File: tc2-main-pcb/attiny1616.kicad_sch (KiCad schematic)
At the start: 20 parts, among them J104 Conn_02x03_Odd_Even, U117 ATtiny1616-M

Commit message: Updated to use field LCSC Part instead of LCSC for the JLCPCB part number
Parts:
- C146, C166: LCSC C16772 -> (none); LCSC Part (none) -> C16772
- C165, C167: LCSC C1555 -> (none); LCSC Part (none) -> C1555
- J104: LCSC C3975129 -> (none); LCSC Part (none) -> C3975129
- R146, R150: LCSC C326730 -> (none); LCSC Part (none) -> C326730
- R147, R151: LCSC C25744 -> (none); LCSC Part (none) -> C25744
- R149: LCSC C25741 -> (none); LCSC Part (none) -> C25741
- R152: LCSC C445619 -> (none); LCSC Part (none) -> C445619
- R153: LCSC C445618 -> (none); LCSC Part (none) -> C445618
- R154, R155, R156: LCSC C11702 -> (none); LCSC Part (none) -> C11702
- R160: LCSC C319591 -> (none); LCSC Part (none) -> C319591
- U117: LCSC C507118 -> (none); LCSC Part (none) -> C507118
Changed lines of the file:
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@@
 			)
 		)
-		(property "LCSC" "C326730"
+		(property "LCSC Part" "C326730"
 			(at 270.51 99.06 0)
 			(effects
@@
 			)
 		)
-		(property "LCSC" "C445618"
+		(property "LCSC Part" "C445618"
 			(at 270.51 118.11 0)
 			(effects
@@
 			)
 		)
-		(property "LCSC" "C11702"
+		(property "LCSC Part" "C11702"
 			(at 62.23 129.54 0)
 			(effects
@@
 			)
 		)
-		(property "LCSC" "C326730"
+		(property "LCSC Part" "C326730"
 			(at 270.51 68.58 0)
 			(effects
@@
 			)
 		)
-		(property "LCSC" "C11702"
+		(property "LCSC Part" "C11702"
 			(at 62.23 124.46 0)
 			(effects
@@
 			)
 		)
-		(property "LCSC" "C445619"
+		(property "LCSC Part" "C445619"
 			(at 270.51 109.22 0)
 			(effects
@@
 			)
 		)
-		(property "LCSC" "C3975129"
+		(property "LCSC Part" "C3975129"
 			(at 215.9 143.51 0)
 			(effects
@@
 			)
 		)
-		(property "LCSC" "C1555"
+		(property "LCSC Part" "C1555"
 			(at 250.19 110.49 0)
 			(effects
@@
 			)
 		)
-		(property "LCSC" "C25744"
+		(property "LCSC Part" "C25744"
 			(at 246.38 73.66 0)
 			(effects
@@
 			)
 		)
-		(property "LCSC" "C16772"
+		(property "LCSC Part" "C16772"
 			(at 224.79 149.86 0)
 			(effects
@@
 			)
 		)
-		(property "LCSC" "C25744"
+		(property "LCSC Part" "C25744"
 			(at 245.11 104.14 0)
 			(effects
@@
 			)
 		)
-		(property "LCSC" "C25741"
+		(property "LCSC Part" "C25741"
 			(at 147.32 93.98 0)
 			(effects
@@
 			)
 		)
-		(property "LCSC" "C16772"
+		(property "LCSC Part" "C16772"
 			(at 106.68 91.44 0)
 			(effects
@@
 			)
 		)
-		(property "LCSC" "C11702"
+		(property "LCSC Part" "C11702"
 			(at 62.23 132.08 0)
 			(effects
@@
 			)
 		)
-		(property "LCSC" "C1555"
+		(property "LCSC Part" "C1555"
 			(at 251.46 78.74 0)
 			(effects
@@
 			)
 		)
-		(property "LCSC" "C319591"
+		(property "LCSC Part" "C319591"
 			(at 270.51 78.74 0)
 			(effects
@@
 			)
 		)
-		(property "LCSC" "C507118"
+		(property "LCSC Part" "C507118"
 			(at 110.49 119.38 0)
 			(effects

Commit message: Tidy up
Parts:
- removed C146: 220nF, Capacitor_SMD:C_0402_1005Metric, symbol Device:C_Small
- removed H107, H108: MountingHole, cacophony-library:MountingHole_2.2mm_M2, symbol Mechanical:MountingHole
- removed J104: Conn_02x03_Odd_Even, cacophony-library:mic-pcb, symbol Connector_Generic:Conn_02x03_Odd_Even
- added LED1: NH-B1515RGBA-HF, cacophony-library:LED-ARRAY-SMD_4P-L1.6-W1.5-TL_NH-B1515RGBA, symbol cacophony-library:NH-B1515RGBA-HF
- added R130, R131, R138: 180Ω, Resistor_SMD:R_0402_1005Metric, symbol Device:R
- added SW1: SW_Push, cacophony-library:SW_PUSH_6mm_11mmh, symbol Switch:SW_Push
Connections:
- net +3V3: now also LED1.2 (+)
- net GND: now also SW1.2
- net ~{LED_B}: now also LED1.3 (-), R138.2; no longer U117.11 (PB3)
- net ~{LED_G}: now also LED1.4 (-), R131.2; no longer U117.12 (PB2)
- net ~{LED_R}: now also LED1.1 (-), R130.2; no longer U117.6 (PA5)
- net ATtiny_SW renamed ATTINY_SW
- net ATTINY_SW: now also SW1.1
- new net LED_B_PHY: R138.1, U117.11 (PB3)
- new net LED_G_PHY: R131.1, U117.12 (PB2)
- new net LED_R_PHY: R130.1, U117.6 (PA5)
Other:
- note removed: "Mounting holes for touch sensor"

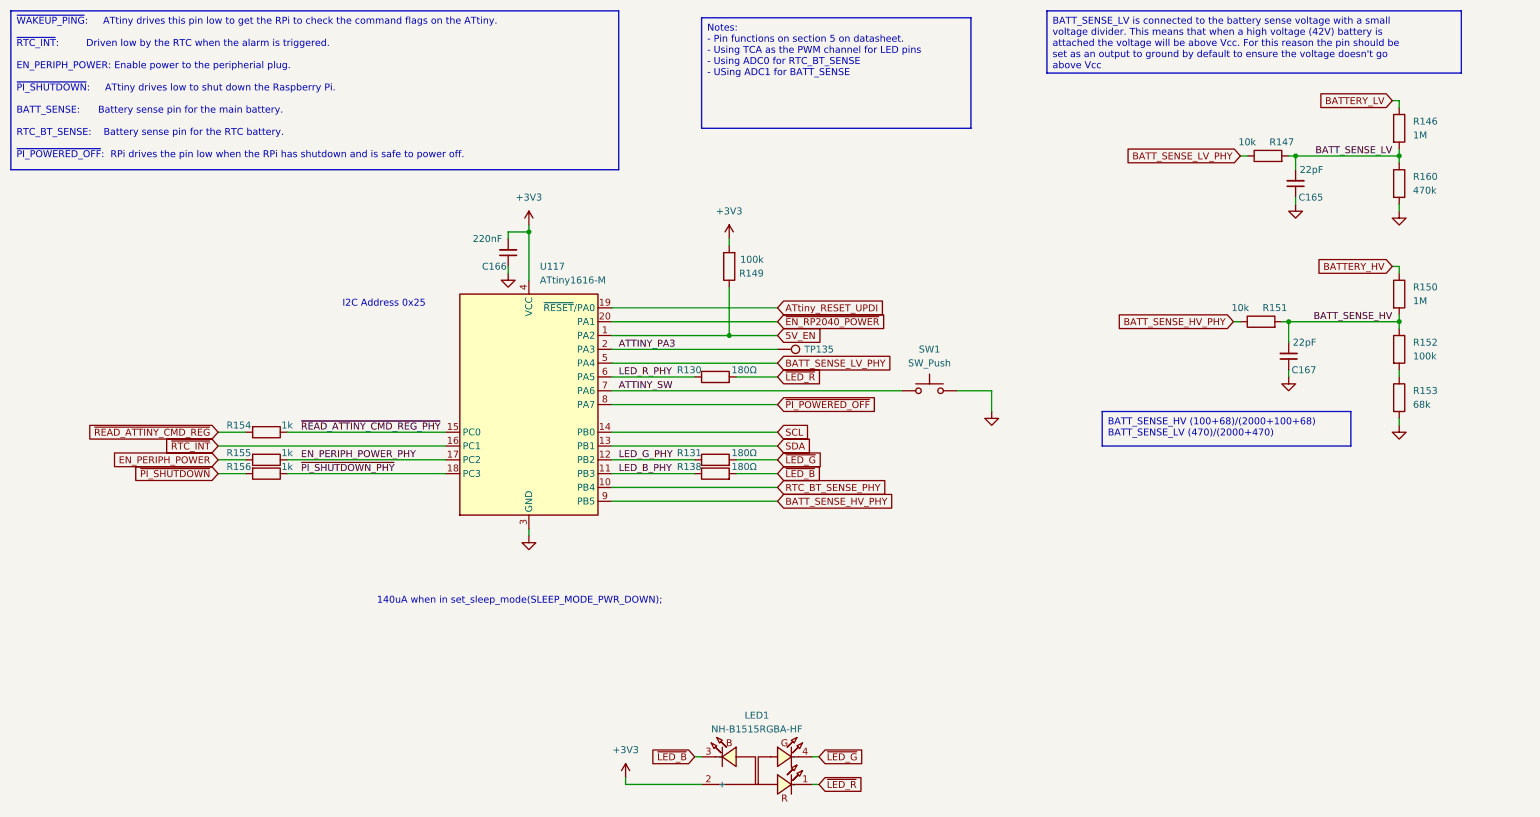
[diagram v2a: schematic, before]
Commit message: Update to kicad 9, fix microphone panel v cuts
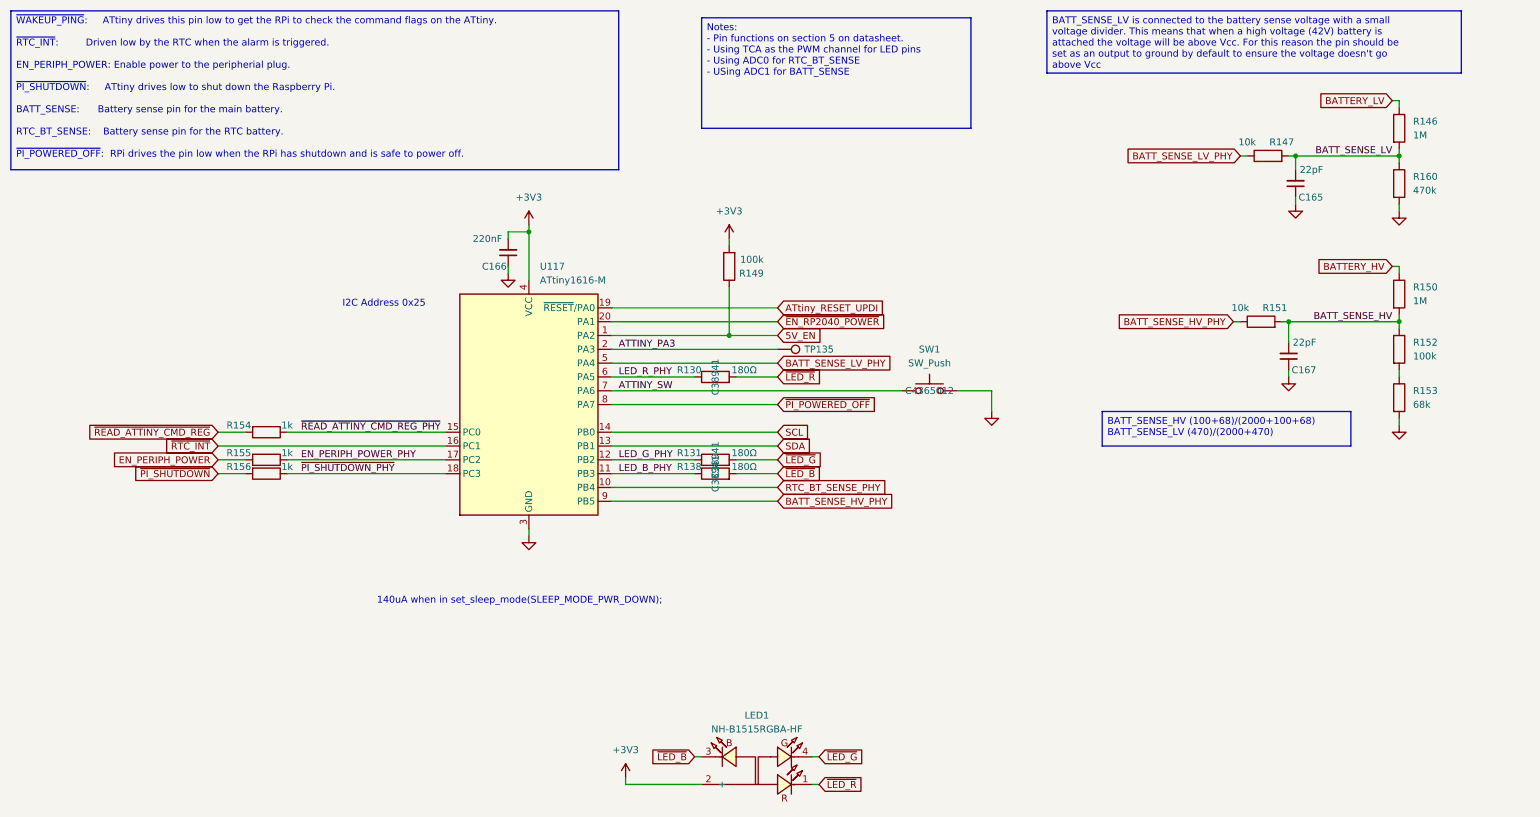
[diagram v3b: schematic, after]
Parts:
- LED1: LCSC C2874115 -> (none); LCSC Part (none) -> C2874115
- R130, R131, R138: LCSC C38941 -> (none); LCSC Part (none) -> C38941
- SW1: LCSC C4365012 -> (none); LCSC Part (none) -> C4365012
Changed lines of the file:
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@@
 (kicad_sch
-	(version 20231120)
+	(version 20250114)
 	(generator "eeschema")
-	(generator_version "8.0")
+	(generator_version "9.0")
 	(paper "A4")
+	(text "140uA when in set_sleep_mode(SLEEP_MODE_PWR_DOWN);"
+		(exclude_from_sim no)
+		(at 82.55 156.21 0)
+		(effects
+			(font
+				(size 1.27 1.27)
+			)
+			(justify left bottom)
+		)
+	)
+	(text "I2C Address 0x25"
+		(exclude_from_sim no)
+		(at 76.2 101.6 0)
+		(effects
+			(font
+				(size 1.27 1.27)
+			)
+			(justify left bottom)
+		)
+	)
+	(text_box "BATT_SENSE_LV is connected to the battery sense voltage with a small voltage divider. This means that when a high voltage (42V) battery is attached the voltage will be above Vcc. For this reason the pin should be set as an output to ground by default to ensure the voltage doesn't go above Vcc"
+		(exclude_from_sim no)
+		(at 205.74 46.99 0)
+		(size 76.2 11.43)
+		(margins 0.9525 0.9525 0.9525 0.9525)
+		(stroke
+			(width 0)
+			(type default)
+		)
+		(fill
+			(type color)
+			(color 255 229 191 1)
+		)
+		(effects
+			(font
+				(size 1.27 1.27)
+			)
+			(justify left top)
+		)
+	)
+	(text_box "BATT_SENSE_HV (100+68)/(2000+100+68)\nBATT_SENSE_LV (470)/(2000+470)"
+		(exclude_from_sim no)
+		(at 215.9 120.65 0)
+		(size 45.72 6.35)
+		(margins 0.9525 0.9525 0.9525 0.9525)
+		(stroke
+			(width 0)
+			(type default)
+		)
+		(fill
+			(type color)
+			(color 255 229 191 1)
+		)
+		(effects
+			(font
+				(size 1.27 1.27)
+			)
+			(justify left top)
+		)
+	)
+	(text_box "~{WAKEUP_PING}:     ATtiny drives this pin low to get the RPi to check the command flags on the ATtiny.\n\n~{RTC_INT}:         Driven low by the RTC when the alarm is triggered.\n\nEN_PERIPH_POWER: Enable power to the peripherial plug.\n\n~{PI_SHUTDOWN}:     ATtiny drives low to shut down the Raspberry Pi.\n\nBATT_SENSE:      Battery sense pin for the main battery.\n\nRTC_BT_SENSE:    Battery sense pin for the RTC battery.\n\n~{PI_POWERED_OFF}:  RPi drives the pin low when the RPi has shutdown and is safe to power off."
+		(exclude_from_sim no)
+		(at 15.24 46.99 0)
+		(size 111.76 29.21)
+		(margins 0.9525 0.9525 0.9525 0.9525)
+		(stroke
+			(width 0)
+			(type default)
+		)
+		(fill
+			(type color)
+			(color 255 229 191 1)
+		)
+		(effects
+			(font
+				(face "DejaVu Sans Mono")
+				(size 1.27 1.27)
+			)
+			(justify left top)
+		)
+	)
+	(text_box "Notes:\n- Pin functions on section 5 on datasheet.\n- Using TCA as the PWM channel for LED pins\n- Using ADC0 for RTC_BT_SENSE\n- USing ADC1 for BATT_SENSE"
+		(exclude_from_sim no)
+		(at 142.24 48.26 0)
+		(size 49.53 20.32)
+		(margins 0.9525 0.9525 0.9525 0.9525)
+		(stroke
+			(width 0)
+			(type default)
+		)
+		(fill
+			(type color)
+			(color 255 229 191 1)
+		)
+		(effects
+			(font
+				(size 1.27 1.27)
+			)
+			(justify left top)
+		)
+	)
 	(junction
 		(at 147.32 106.68)
@@
 		)
 	)
-	(text_box "BATT_SENSE_LV is connected to the battery sense voltage with a small voltage divider. This means that when a high voltage (42V) battery is attached the voltage will be above Vcc. For this reason the pin should be set as an output to ground by default to ensure the voltage doesn't go above Vcc"
-		(exclude_from_sim no)
-		(at 205.74 46.99 0)
-		(size 76.2 11.43)
-		(stroke
-			(width 0)
-			(type default)
-		)
-		(fill
-			(type color)
-			(color 255 229 191 1)
-		)
-		(effects
-			(font
-				(size 1.27 1.27)
-			)
-			(justify left top)
-		)
-	)
-	(text_box "BATT_SENSE_HV (100+68)/(2000+100+68)\nBATT_SENSE_LV (470)/(2000+470)"
-		(exclude_from_sim no)
-		(at 215.9 120.65 0)
-		(size 45.72 6.35)
-		(stroke
-			(width 0)
-			(type default)
-		)
-		(fill
-			(type color)
-			(color 255 229 191 1)
-		)
-		(effects
-			(font
-				(size 1.27 1.27)
-			)
-			(justify left top)
-		)
-	)
-	(text_box "~{WAKEUP_PING}:     ATtiny drives this pin low to get the RPi to check the command flags on the ATtiny.\n\n~{RTC_INT}:         Driven low by the RTC when the alarm is triggered.\n\nEN_PERIPH_POWER: Enable power to the peripherial plug.\n\n~{PI_SHUTDOWN}:     ATtiny drives low to shut down the Raspberry Pi.\n\nBATT_SENSE:      Battery sense pin for the main battery.\n\nRTC_BT_SENSE:    Battery sense pin for the RTC battery.\n\n~{PI_POWERED_OFF}:  RPi drives the pin low when the RPi has shutdown and is safe to power off."
-		(exclude_from_sim no)
-		(at 15.24 46.99 0)
-		(size 111.76 29.21)
-		(stroke
-			(width 0)
-			(type default)
-		)
-		(fill
-			(type color)
-			(color 255 229 191 1)
-		)
-		(effects
-			(font
-				(face "DejaVu Sans Mono")
-				(size 1.27 1.27)
-			)
-			(justify left top)
-		)
-	)
-	(text_box "Notes:\n- Pin functions on section 5 on datasheet.\n- Using TCA as the PWM channel for LED pins\n- Using ADC0 for RTC_BT_SENSE\n- USing ADC1 for BATT_SENSE"
-		(exclude_from_sim no)
-		(at 142.24 48.26 0)
-		(size 49.53 20.32)
-		(stroke
-			(width 0)
-			(type default)
-		)
-		(fill
-			(type color)
-			(color 255 229 191 1)
-		)
-		(effects
-			(font
-				(size 1.27 1.27)
-			)
-			(justify left top)
-		)
-	)
-	(text "140uA when in set_sleep_mode(SLEEP_MODE_PWR_DOWN);"
-		(exclude_from_sim no)
-		(at 82.55 156.21 0)
-		(effects
-			(font
-				(size 1.27 1.27)
-			)
-			(justify left bottom)
-		)
-	)
-	(text "I2C Address 0x25"
-		(exclude_from_sim no)
-		(at 76.2 101.6 0)
-		(effects
-			(font
-				(size 1.27 1.27)
-			)
-			(justify left bottom)
-		)
-	)
 	(label "BATT_SENSE_HV"
 		(at 269.24 104.14 180)
@@
 			)
 		)
-		(property "LCSC" "C38941"
+		(property "LCSC" ""
 			(at 144.78 132.08 0)
 			(effects
@@
 			)
 		)
+		(property "LCSC Part" "C38941"
+			(at 144.78 132.08 0)
+			(effects
+				(font
+					(size 1.27 1.27)
+				)
+			)
+		)
 		(pin "1"
 		)
@@
 			)
 		)
-		(property "LCSC" "C38941"
+		(property "LCSC" ""
 			(at 144.78 114.3 0)
 			(effects
@@
 			)
 		)
+		(property "LCSC Part" "C38941"
+			(at 144.78 114.3 0)
+			(effects
+				(font
+					(size 1.27 1.27)
+				)
+			)
+		)
 		(pin "1"
 		)
@@
 			)
 		)
-		(property "LCSC" "C4365012"
+		(property "JLC Part" ""
 			(at 184.15 116.84 0)
 			(effects
@@
 			)
 		)
+		(property "LCSC Part" "C4365012"
+			(at 184.15 116.84 0)
+			(effects
+				(font
+					(size 1.27 1.27)
+				)
+			)
+		)
 		(pin "2"
 		)
@@
 			)
 		)
-		(property "LCSC" "C38941"
+		(property "LCSC" ""
 			(at 144.78 129.54 0)
 			(effects
@@
 			)
 		)
+		(property "LCSC Part" "C38941"
+			(at 144.78 129.54 0)
+			(effects
+				(font
+					(size 1.27 1.27)
+				)
+			)
+		)
 		(pin "1"
 		)
@@
 			)
 		)
-		(property "LCSC Part" ""
+		(property "LCSC Part" "C2874115"
 			(at 152.4 201.93 0)
 			(effects
@@
 			)
 		)
-		(property "LCSC" "C2874115"
+		(property "LCSC" ""
 			(at 152.4 186.69 0)
 			(effects
